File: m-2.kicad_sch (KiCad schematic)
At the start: 61 parts, among them J1 2199230-6, J2 1-2199230-6, M2 M2_4222, M3 M2_2280, U2 74LVC2G07GV, U3 74LVC2G07GV, Y1 ECS-327MVATX-2-CN-TR3

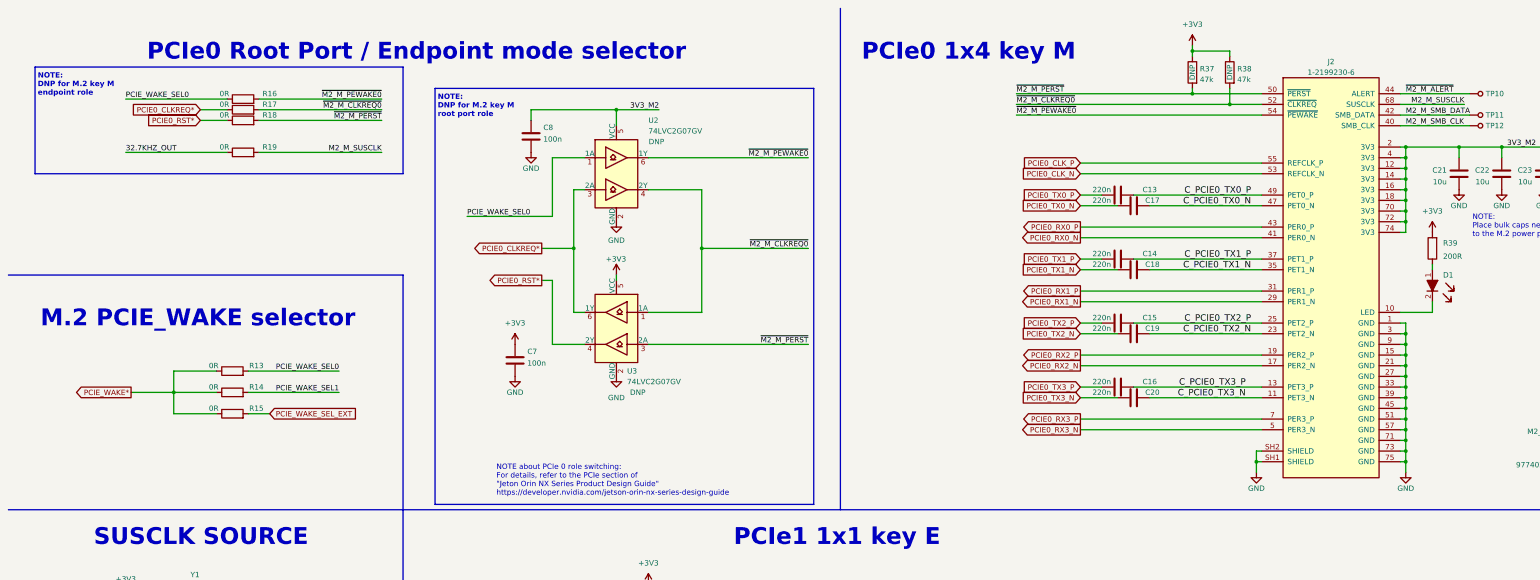
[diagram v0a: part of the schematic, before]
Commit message: PCIE Simplification finished
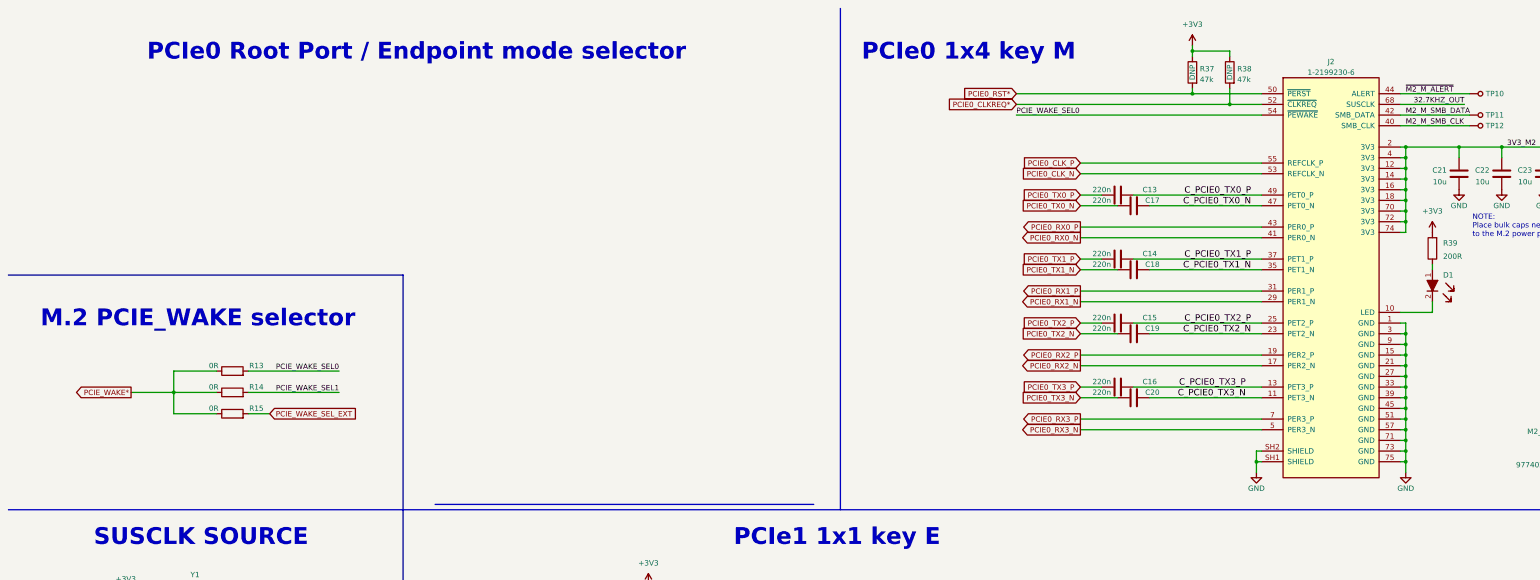
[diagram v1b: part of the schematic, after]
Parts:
- removed C7, C8: C_100n_0402, jetson-orin-baseboard-footprints:0402-cap, symbol jetson-orin-baseboard:C_100n_0402
- removed R16, R17, R18, R19: R_0R_0402, jetson-orin-baseboard-footprints:0402-res, symbol jetson-orin-baseboard:R_0R_0402
- removed U2, U3: 74LVC2G07GV, jetson-orin-baseboard-footprints:SC-74, symbol jetson-orin-baseboard:74LVC2G07GV
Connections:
- net M2_M_SUSCLK is gone; now on net 32.7KHZ_OUT: J2.68 (SUSCLK)
- net ~{M2_M_CLKREQ0} is gone; now on net PCIE0_CLKREQ*: J2.52 (~{CLKREQ}), R38.2
- net ~{M2_M_PERST} is gone; now on net PCIE0_RST*: J2.50 (~{PERST}), R37.2
- net ~{M2_M_PEWAKE0} is gone; now on net PCIE_WAKE_SEL0: J2.54 (~{PEWAKE})
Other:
- note removed: "NOTE about PCIe 0 role switching: For details, refer to the PCIe section of "Jeton Orin NX Series Product Design Guide" https://developer.nvidia.com/jetson-orin-nx-series-design-guide"
- note removed: "NOTE: DNP for M.2 key M endpoint role"
- note removed: "NOTE: DNP for M.2 key M root port role"
- company: Antmicro Ltd -> Dronolab
- title: Jetson Orin Baseboard -> M.2

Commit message: Simplification continues
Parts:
- removed C10, C9: C_220n_0402, jetson-orin-baseboard-footprints:0402-cap, symbol jetson-orin-baseboard:C_220n_0402
- removed C11, C12: C_10u_0603, jetson-orin-baseboard-footprints:0603-cap, symbol jetson-orin-baseboard:C_10u_0603
- removed D51, D52: LTST-C190GKT, jetson-orin-baseboard-footprints:LED_0603, symbol jetson-orin-baseboard:LTST-C190GKT
- removed J1: 2199230-6, jetson-orin-baseboard-footprints:2199230-4, symbol jetson-orin-baseboard:2199230-6
- removed M2: M2_4222, jetson-orin-baseboard-footprints:m2_4222, symbol jetson-orin-baseboard:M2_4222
- removed R13, R14, R15, R20, R29, R30, R31, R52: R_0R_0402, jetson-orin-baseboard-footprints:0402-res, symbol jetson-orin-baseboard:R_0R_0402
- removed R186, R187: R_200R_0402, jetson-orin-baseboard-footprints:0402-res, symbol jetson-orin-baseboard:R_200R_0402
- removed R21, R22: 4x0R_0201_array, jetson-orin-baseboard-footprints:EXB18V, symbol jetson-orin-baseboard:4x0R_0201_array
- removed R27, R28, R32: R_47k_0402, jetson-orin-baseboard-footprints:0402-res, symbol jetson-orin-baseboard:R_47k_0402
- removed SP7: 9774025151, jetson-orin-baseboard-footprints:9774025151, symbol jetson-orin-baseboard:9774025151
- removed TP6, TP7, TP8, TP9: TP_SMD_0_75MM, jetson-orin-baseboard-footprints:Testpoint_smd_0_75mm, symbol jetson-orin-baseboard:TP_SMD_0_75MM
- added R13, R14, R15: 0, symbol Device:R
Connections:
- net +3V3: now also R14.1
- net GND: now also R15.1
- net PCIE_WAKE*: now also R13.1
- net PCIE_WAKE_SEL0: no longer names the net of J2.54 (~{PEWAKE})
- net PCIE_WAKE_SEL0: now also R13.2, R14.2, R15.2
- no-connect marks 23 -> 0
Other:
- note removed: "BT"
- note removed: "M.2 PCIE_WAKE selector"
- note removed: "PCIe0 Root Port / Endpoint mode selector"
- note removed: "PCIe1 1x1 key E"
- note removed: "WLAN"
- moved on the sheet: C13, C14, C15, C16, C17, C18, C19, C20, C21, C22, C23, C24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

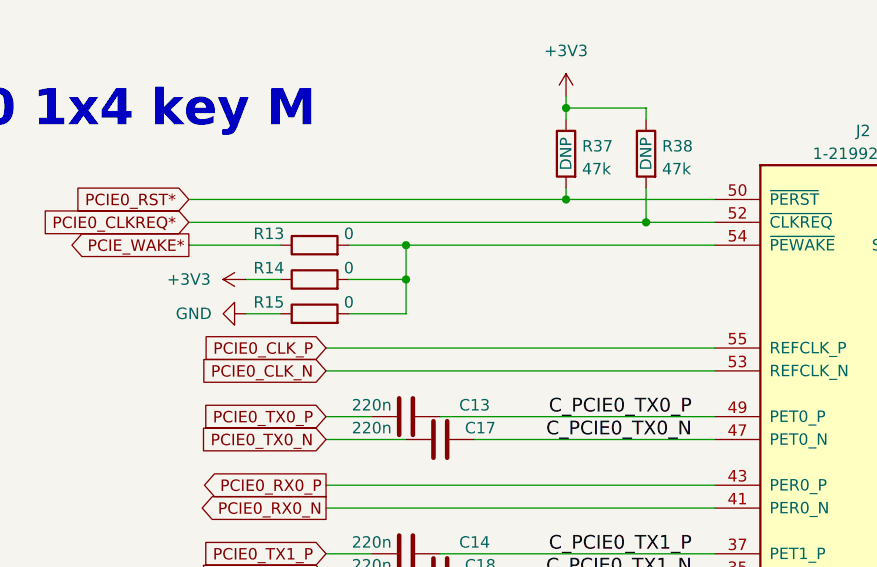
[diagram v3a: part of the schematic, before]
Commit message: Schematic check
Include Pinmux and Schematic Check excels in doc folder and doing a lot of checking and correcting things.
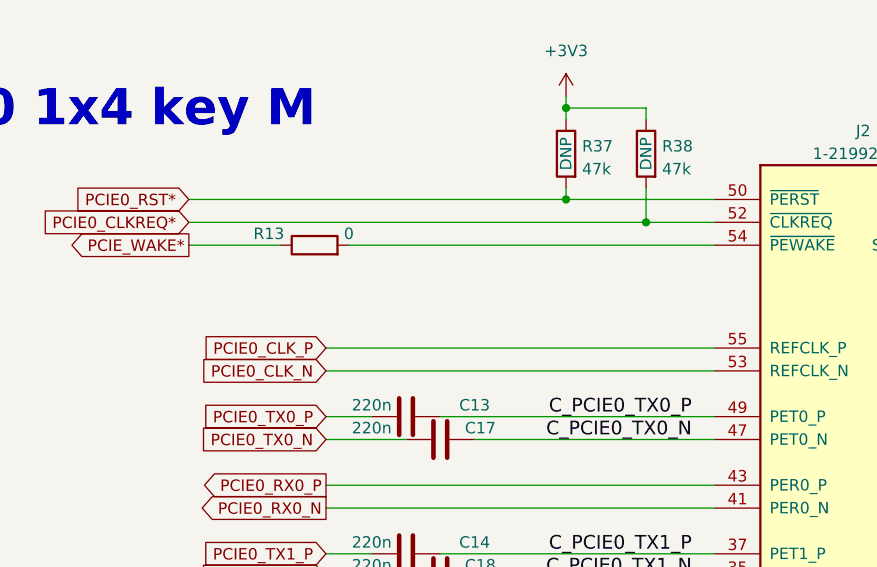
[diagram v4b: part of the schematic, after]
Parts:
- removed R14, R15: 0, symbol Device:R
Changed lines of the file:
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@@
   (junction (at 248.92 142.24) (diameter 0) (color 0 0 0 0)
   )
-  (junction (at 167.64 138.43) (diameter 0) (color 0 0 0 0)
-  )
   (junction (at 236.22 194.31) (diameter 0) (color 0 0 0 0)
   )
@@
   (junction (at 236.22 204.47) (diameter 0) (color 0 0 0 0)
   )
-  (junction (at 167.64 134.62) (diameter 0) (color 0 0 0 0)
-  )
   (junction (at 236.22 142.24) (diameter 0) (color 0 0 0 0)
   )
@@
     (stroke (width 0) (type default))
   )
-  (wire (pts (xy 161.29 142.24) (xy 167.64 142.24))
-    (stroke (width 0) (type default))
-  )
   (wire (pts (xy 236.22 160.02) (xy 236.22 162.56))
     (stroke (width 0) (type default))
@@
     (stroke (width 0) (type default))
   )
-  (wire (pts (xy 167.64 138.43) (xy 167.64 134.62))
-    (stroke (width 0) (type default))
-  )
   (wire (pts (xy 163.83 168.91) (xy 158.75 168.91))
     (stroke (width 0) (type default))
@@
     (stroke (width 0) (type default))
   )
-  (wire (pts (xy 167.64 138.43) (xy 167.64 142.24))
-    (stroke (width 0) (type default))
-  )
   (wire (pts (xy 234.95 214.63) (xy 236.22 214.63))
     (stroke (width 0) (type default))
@@
     (stroke (width 0) (type default))
   )
-  (wire (pts (xy 149.86 138.43) (xy 153.67 138.43))
-    (stroke (width 0) (type default))
-  )
   (wire (pts (xy 236.22 199.39) (xy 236.22 201.93))
     (stroke (width 0) (type default))
@@
     (stroke (width 0) (type default))
   )
-  (wire (pts (xy 149.86 142.24) (xy 153.67 142.24))
-    (stroke (width 0) (type default))
-  )
   (wire (pts (xy 236.22 217.17) (xy 236.22 219.71))
     (stroke (width 0) (type default))
@@
     (stroke (width 0) (type default))
   )
-  (wire (pts (xy 161.29 138.43) (xy 167.64 138.43))
-    (stroke (width 0) (type default))
-  )
   (wire (pts (xy 236.22 149.86) (xy 236.22 152.4))
     (stroke (width 0) (type default))
@@
     (stroke (width 0) (type default))
   )
-  (wire (pts (xy 167.64 134.62) (xy 201.93 134.62))
+  (wire (pts (xy 161.29 134.62) (xy 201.93 134.62))
     (stroke (width 0) (type default))
   )
@@
     (stroke (width 0) (type default))
   )
-  (wire (pts (xy 161.29 134.62) (xy 167.64 134.62))
-    (stroke (width 0) (type default))
-  )
   (wire (pts (xy 234.95 149.86) (xy 236.22 149.86))
     (stroke (width 0) (type default))
@@
     )
   )
-  (symbol (lib_id "Device:R") (at 157.48 142.24 90) (unit 1)
-    (in_bom yes) (on_board yes) (dnp no)
-    (property "Reference" "R15" (at 152.4 140.97 90)
-      (effects (font (size 1.27 1.27)))
-    )
-    (property "Value" "0" (at 161.29 140.97 90)
-      (effects (font (size 1.27 1.27)))
-    )
-    (property "Footprint" "" (at 157.48 144.018 90)
-      (effects (font (size 1.27 1.27)) hide)
-    )
-    (property "Datasheet" "~" (at 157.48 142.24 0)
-      (effects (font (size 1.27 1.27)) hide)
-    )
-    (pin "1")
-    (pin "2")
-    (instances
-      (project "jetson-orin-baseboard"
-        (path "/4b393452-b11e-416e-bc83-918ae3cab2f1/8161d945-5864-43d7-8197-061df5f04897"
-          (reference "R15") (unit 1)
-        )
-      )
-    )
-  )
   (symbol (lib_id "jetson-orin-baseboard:GND") (at 200.66 219.71 0) (unit 1)
     (in_bom yes) (on_board yes) (dnp no) (fields_autoplaced)
@@
     )
   )
-  (symbol (lib_id "jetson-orin-baseboard:GND") (at 149.86 142.24 270) (unit 1)
-    (in_bom yes) (on_board yes) (dnp no) (fields_autoplaced)
-    (property "Reference" "#PWR021" (at 143.51 142.24 0)
-      (effects (font (size 1.27 1.27)) hide)
-    )
-    (property "Value" "GND" (at 146.05 142.24 90)
-      (effects (font (size 1.27 1.27)) (justify right))
-    )
-    (property "Footprint" "" (at 149.86 142.24 0)
-      (effects (font (size 1.27 1.27)) hide)
-    )
-    (property "Datasheet" "" (at 149.86 142.24 0)
-      (effects (font (size 1.27 1.27)) hide)
-    )
-    (pin "1")
-    (instances
-      (project "jetson-orin-baseboard"
-        (path "/4b393452-b11e-416e-bc83-918ae3cab2f1/8161d945-5864-43d7-8197-061df5f04897"
-          (reference "#PWR021") (unit 1)
-        )
-      )
-    )
-  )
   (symbol (lib_id "jetson-orin-baseboard:GND") (at 236.22 219.71 0) (unit 1)
     (in_bom yes) (on_board yes) (dnp no) (fields_autoplaced)
@@
     )
   )
-  (symbol (lib_id "Device:R") (at 157.48 138.43 90) (unit 1)
-    (in_bom yes) (on_board yes) (dnp no)
-    (property "Reference" "R14" (at 152.4 137.16 90)
-      (effects (font (size 1.27 1.27)))
-    )
-    (property "Value" "0" (at 161.29 137.16 90)
-      (effects (font (size 1.27 1.27)))
-    )
-    (property "Footprint" "" (at 157.48 140.208 90)
-      (effects (font (size 1.27 1.27)) hide)
-    )
-    (property "Datasheet" "~" (at 157.48 138.43 0)
-      (effects (font (size 1.27 1.27)) hide)
-    )
-    (pin "1")
-    (pin "2")
-    (instances
-      (project "jetson-orin-baseboard"
-        (path "/4b393452-b11e-416e-bc83-918ae3cab2f1/8161d945-5864-43d7-8197-061df5f04897"
-          (reference "R14") (unit 1)
-        )
-      )
-    )
-  )
   (symbol (lib_id "jetson-orin-baseboard:C_220n_0402") (at 167.64 153.67 90) (unit 1)
     (in_bom yes) (on_board yes) (dnp no)
@@
         )
       )
-    )
-  )
-  (symbol (lib_id "jetson-orin-baseboard:+3V3") (at 149.86 138.43 90) (unit 1)
-    (in_bom yes) (on_board yes) (dnp no)
-    (property "Reference" "#PWR020" (at 153.67 138.43 0)
-      (effects (font (size 1.27 1.27)) hide)
-    )
-    (property "Value" "+3V3" (at 143.51 138.43 90)
-      (effects (font (size 1.27 1.27)))
-    )
-    (property "Footprint" "" (at 149.86 138.43 0)
-      (effects (font (size 1.27 1.27)) hide)
-    )
-    (property "Datasheet" "" (at 149.86 138.43 0)
-      (effects (font (size 1.27 1.27)) hide)
-    )
-    (pin "1")
-    (instances
-      (project "jetson-orin-baseboard"
-        (path "/4b393452-b11e-416e-bc83-918ae3cab2f1/8161d945-5864-43d7-8197-061df5f04897"
-          (reference "#PWR020") (unit 1)
-        )
-      )
